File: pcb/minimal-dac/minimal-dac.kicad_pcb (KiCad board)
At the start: 6 parts, among them J1 PinHeader_2x06_P2.54mm, U1 AD5754

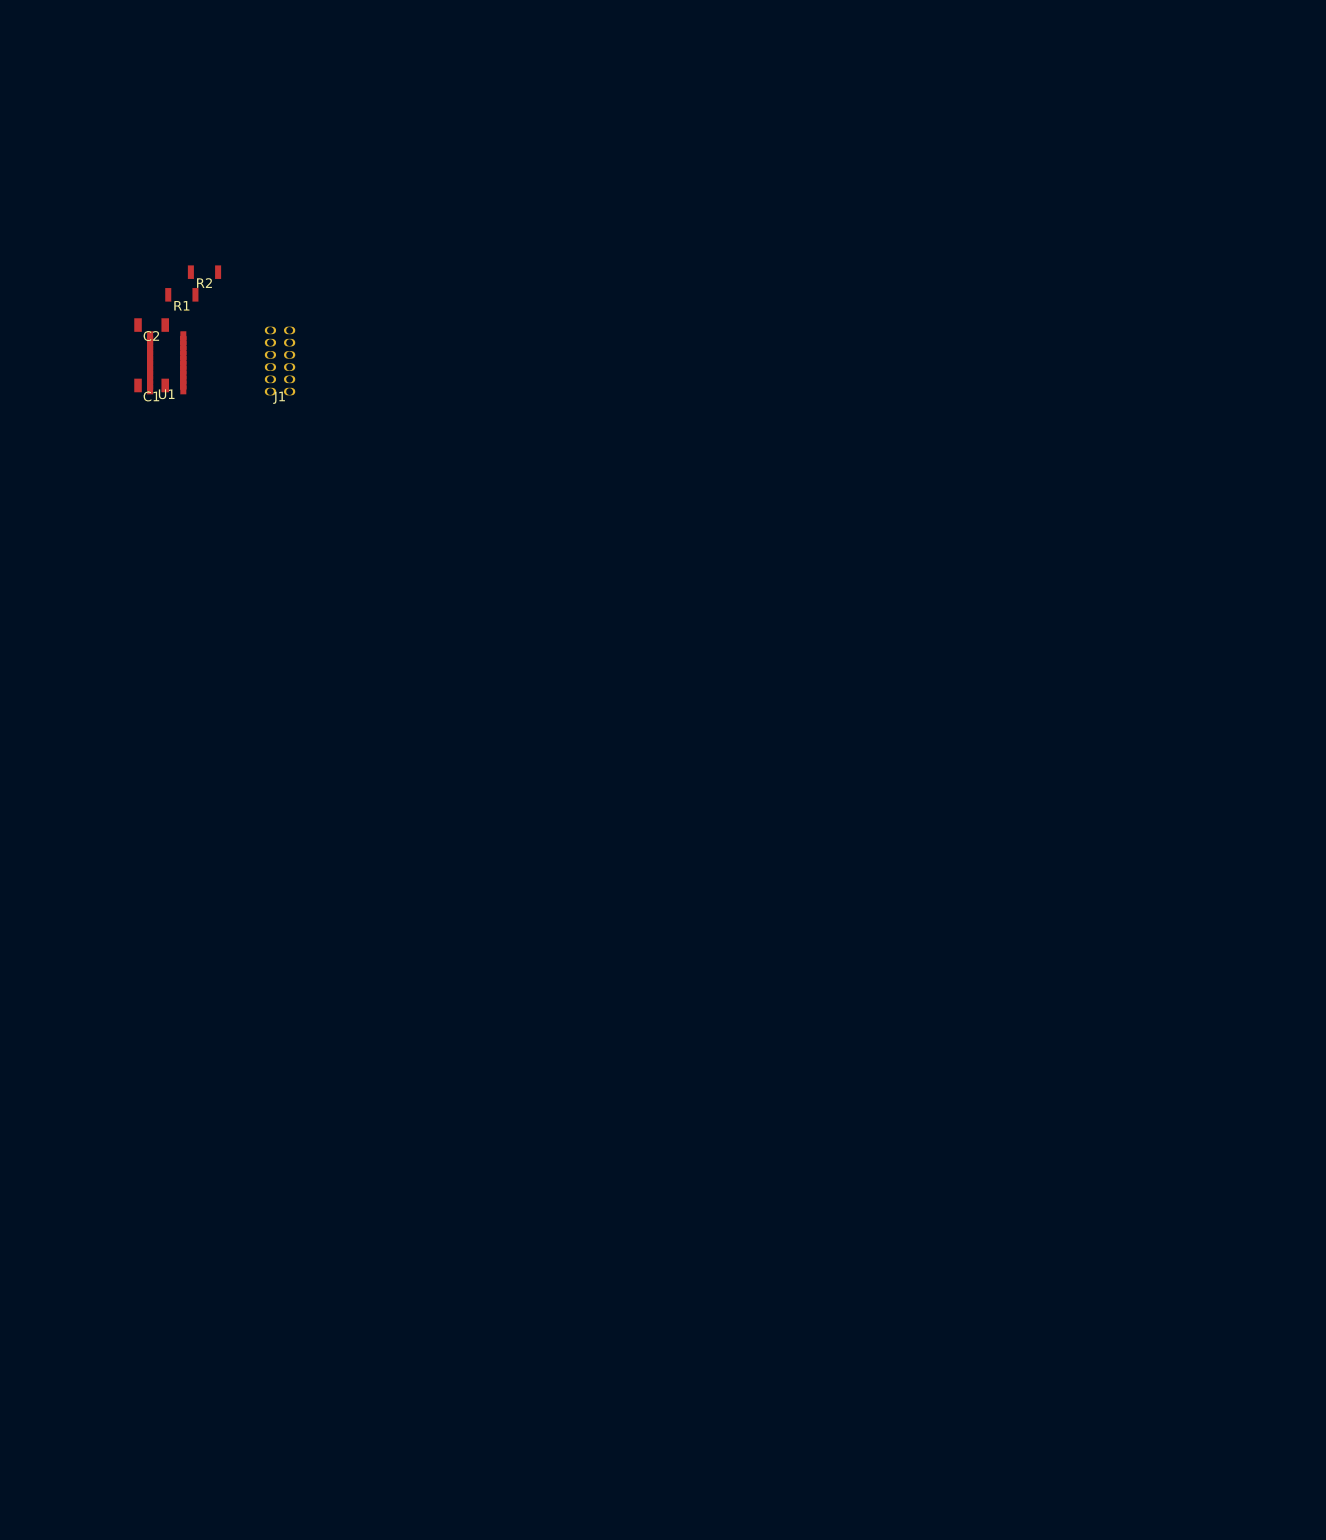
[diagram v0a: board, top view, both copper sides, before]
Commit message: AD5754 pcb en elements gedachten
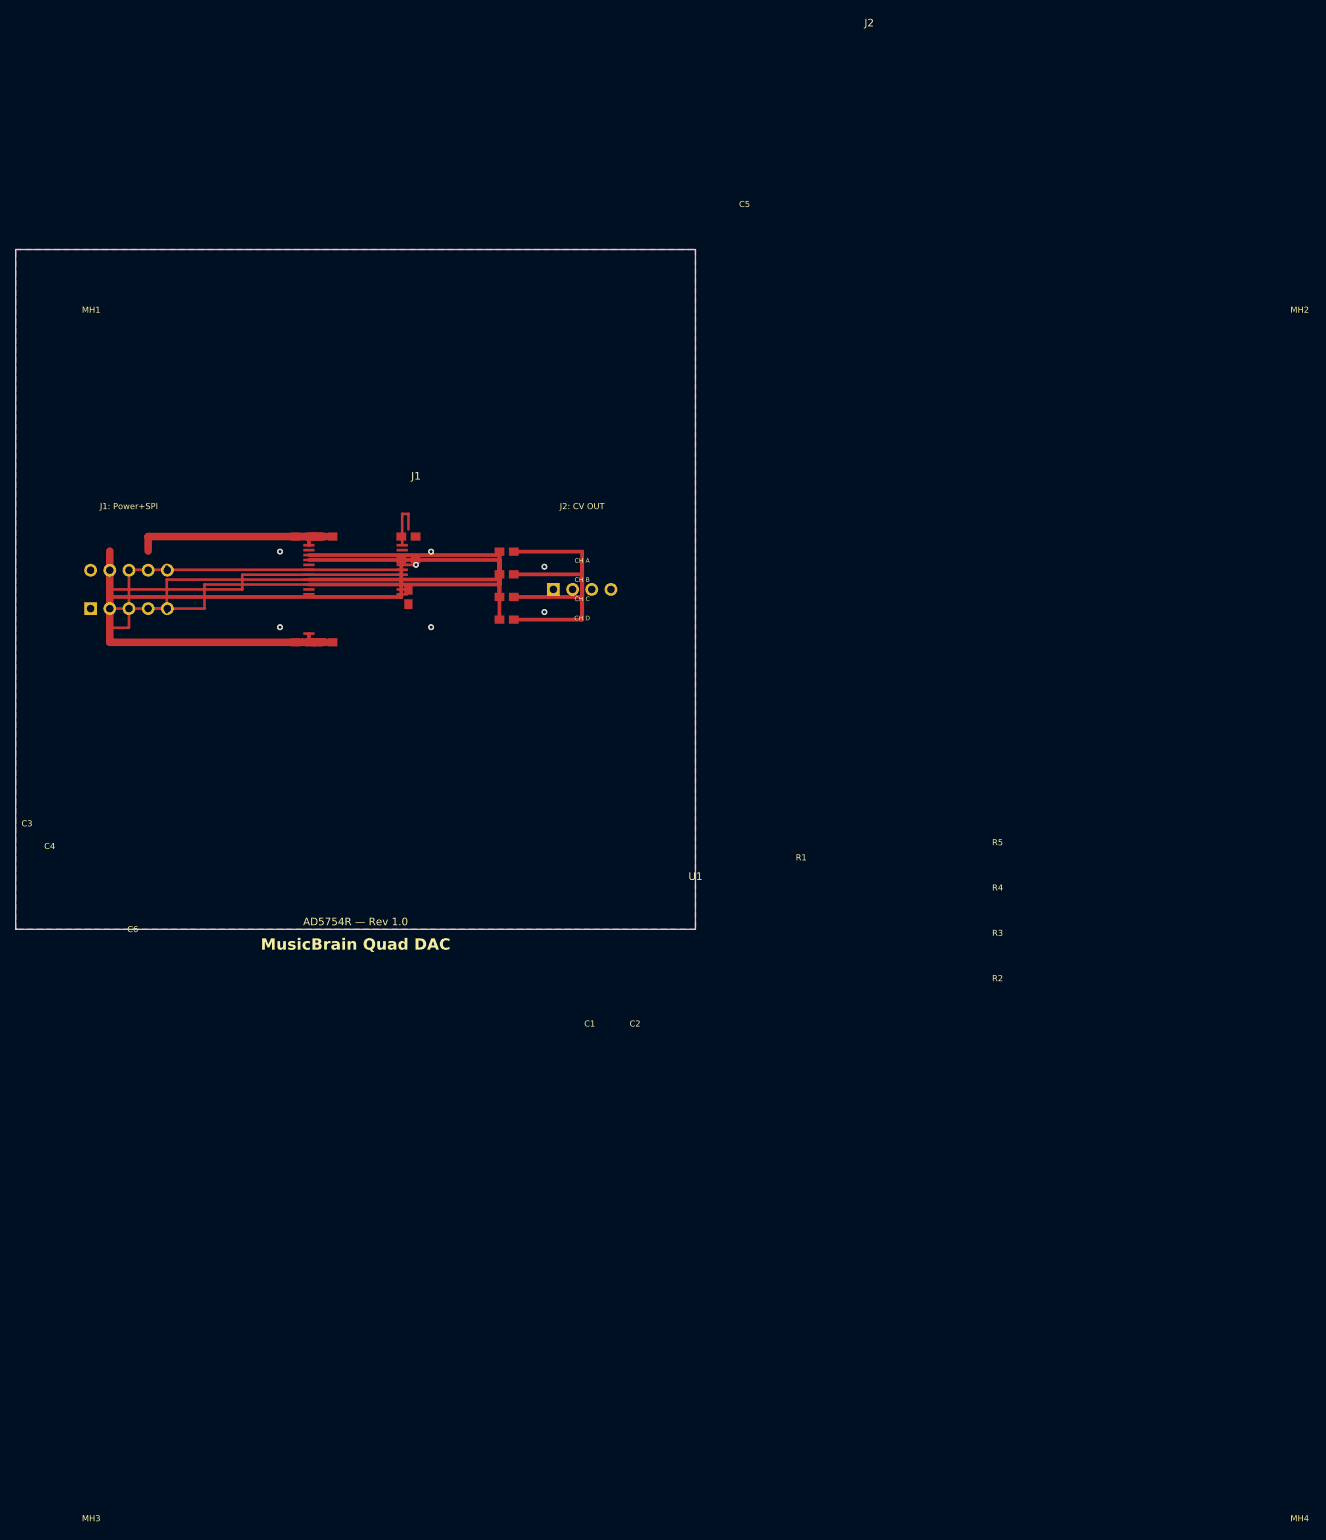
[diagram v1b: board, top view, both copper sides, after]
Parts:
- added C3: 10µF, Capacitor_SMD:C_0805_2012Metric, F.Cu at (38.0, 38.0)
- added C4: 0.1µF, Capacitor_SMD:C_0805_2012Metric, F.Cu at (41.0, 38.0)
- added C5: 0.1µF, Capacitor_SMD:C_0805_2012Metric, F.Cu at (52.0, 46.0)
- added C6: 0.1µF, Capacitor_SMD:C_0805_2012Metric, F.Cu at (52.0, 38.0)
- added J2: CV_OUT, Connector_PinHeader_2.54mm:PinHeader_1x04_P2.54mm_Vertical, F.Cu at (75.0, 45.0)
- added MH1: , MountingHole:MountingHole_3.2mm_M3, F.Cu at (5.00, 5.00)
- added MH2: , MountingHole:MountingHole_3.2mm_M3, F.Cu at (85.0, 5.00)
- added MH3: , MountingHole:MountingHole_3.2mm_M3, F.Cu at (5.00, 85.0)
- added MH4: , MountingHole:MountingHole_3.2mm_M3, F.Cu at (85.0, 85.0)
- added R3: 47Ω, Resistor_SMD:R_0805_2012Metric, F.Cu at (65.0, 46.0)
- added R4: 47Ω, Resistor_SMD:R_0805_2012Metric, F.Cu at (65.0, 43.0)
- added R5: 47Ω, Resistor_SMD:R_0805_2012Metric, F.Cu at (65.0, 40.0)
- C1: value 0.1uF -> 10µF
- C2: value 10uF -> 0.1µF
- J1: value PinHeader_2x06_P2.54mm -> Power+SPI; footprint Connector_PinHeader_2.54mm:PinHeader_2x06_P2.54mm_Vertical -> Connector_PinHeader_2.54mm:PinHeader_2x05_P2.54mm_Vertical
- R1: value 10k -> 10kΩ
- R2: value 47R -> 47Ω
- U1: value AD5754 -> AD5754R
- moved R2 61.0 mm to (65.0, 49.0)
- moved C2 47.9 mm to (41.0, 52.0)
- moved R1 46.1 mm to (52.0, 41.0)
- moved C1 39.4 mm to (38.0, 52.0)
- moved U1 39.1 mm to (45.0, 45.0)
- moved J1 36.1 mm to (15.0, 45.0), turned to 90 degrees
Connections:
- C1 pad 1: +3V3 -> +12V
- J1 pad 10: VOUT_B -> GND
- J1 pad 3: GND -> +3V3
- J1 pad 4: +3V3 -> GND
- J1 pad 5: SCK -> MOSI
- J1 pad 6: MOSI -> GND
- J1 pad 7: MISO -> SCK
- J1 pad 8: CS -> MISO
- J1 pad 9: VOUT_A -> CS
- R1 pad 1: CLR -> +3V3
- R1 pad 2: +3V3 -> CLR
- R2 pad 2: GND -> VOUT_A
- U1 pad 14: GND -> SCK
- U1 pad 15: REFIN -> MISO
- U1 pad 16: GND -> MOSI
- U1 pad 20: GND -> (no net)
- U1 pad 22: SCK -> REFIN
- U1 pad 23: MISO -> GND
- U1 pad 24: MOSI -> +12V
- U1 pad 7: VOUT_C -> (no net)
- U1 pad 8: VOUT_D -> VOUT_C
- U1 pad 9: (no net) -> VOUT_D
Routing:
- net VOUT_A: track 0.00 -> 50.6 mm
- net +3V3: track 0.00 -> 47.6 mm
- net VOUT_D: track 0.00 -> 47.4 mm
- net CS: track 0.00 -> 46.4 mm
- net +12V: track 0.00 -> 43.9 mm
- net SCK: track 0.00 -> 41.9 mm
- net VOUT_B: track 0.00 -> 41.4 mm
- net MOSI: track 0.00 -> 40.7 mm
- net VOUT_C: track 0.00 -> 38.2 mm
- net MISO: track 0.00 -> 37.5 mm
- net -12V: track 0.00 -> 28.7 mm
- net REFIN: track 0.00 -> 7.02 mm
- net CLR: track 0.00 -> 1.88 mm
- net GND: track 0.00 -> 1.83 mm, vias 0 -> 9
- added copper zone on B.Cu, net GND
- added copper zone on F.Cu, net GND
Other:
- board outline added: 90 x 90 mm
- copper layers 0 -> 2
- rule pad_to_mask_clearance: 0.04 -> 0.05
- board text added: "AD5754R — Rev 1.0"
- board text added: "CH A"
- board text added: "CH B"
- board text added: "CH C"
- board text added: "CH D"
- board text added: "J1: Power+SPI"
- board text added: "J2: CV OUT"
- board text added: "JLCPCB 2-layer 1.6mm FR4"
- board text added: "MusicBrain Quad DAC"

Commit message: pcbs
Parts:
- U1: value AD5754R -> AD5754BREZ
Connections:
- U1 pad 11: GND -> CLR
- U1 pad 12: +3V3 -> (no net)
- U1 pad 13: GND -> (no net)
- U1 pad 14: SCK -> +3V3
- U1 pad 15: MISO -> GND
- U1 pad 16: MOSI -> MISO
- U1 pad 17: CS -> REFIN
- U1 pad 19: CLR -> GND
- U1 pad 2: GND -> (no net)
- U1 pad 20: (no net) -> GND
- U1 pad 22: REFIN -> VOUT_D
- U1 pad 23: GND -> VOUT_C
- U1 pad 7: (no net) -> CS
- U1 pad 8: VOUT_C -> SCK
- U1 pad 9: VOUT_D -> MOSI
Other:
- board text added: "AD5754BREZ — Rev 1.0"
- board text removed: "AD5754R — Rev 1.0"
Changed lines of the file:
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@@
   (layers
     (0 "F.Cu" signal)
-    (1 "In1.Cu" dielectric 1)
-    (2 "In2.Cu" dielectric 2)
+    (1 "In1.Cu" dielectric)
+    (2 "In2.Cu" dielectric)
     (3 "B.Cu" signal)
     (4 "F.Adhes" user "Adhesive on front")
@@
   ;; Footprints
   ;; =========================================================================
-  ;; ── U1: AD5754R — TSSOP-24 ────────────────────────────────────────────
+  ;; ── U1: AD5754BREZ — TSSOP-24 ────────────────────────────────────────────
   (footprint "Package_SO:TSSOP-24_4.4x7.8mm_P0.65mm"
     (layer "F.Cu")
@@
     (property "Reference" "U1" (at 45 38 0) (layer "F.SilkS")
       (effects (font (size 1.0 1.0) (thickness 0.15))))
-    (property "Value" "AD5754R" (at 45 52 0) (layer "F.Fab")
+    (property "Value" "AD5754BREZ" (at 45 52 0) (layer "F.Fab")
       (effects (font (size 1.0 1.0) (thickness 0.15))))
     (pad "1" smd rect (at -6.175 -5.85 0) (size 1.5 0.35) (layers "F.Cu" "F.Paste" "F.Mask") (net 2))
-    (pad "2" smd rect (at -6.175 -5.2 0) (size 1.5 0.35) (layers "F.Cu" "F.Paste" "F.Mask") (net 4))
+    (pad "2" smd rect (at -6.175 -5.2 0) (size 1.5 0.35) (layers "F.Cu" "F.Paste" "F.Mask") (net 0))
     (pad "3" smd rect (at -6.175 -4.55 0) (size 1.5 0.35) (layers "F.Cu" "F.Paste" "F.Mask") (net 9))
     (pad "4" smd rect (at -6.175 -3.9 0) (size 1.5 0.35) (layers "F.Cu" "F.Paste" "F.Mask") (net 10))
     (pad "5" smd rect (at -6.175 -3.25 0) (size 1.5 0.35) (layers "F.Cu" "F.Paste" "F.Mask") (net 0))
     (pad "6" smd rect (at -6.175 -2.6 0) (size 1.5 0.35) (layers "F.Cu" "F.Paste" "F.Mask") (net 0))
-    (pad "7" smd rect (at -6.175 -1.95 0) (size 1.5 0.35) (layers "F.Cu" "F.Paste" "F.Mask") (net 0))
-    (pad "8" smd rect (at -6.175 -1.3 0) (size 1.5 0.35) (layers "F.Cu" "F.Paste" "F.Mask") (net 11))
-    (pad "9" smd rect (at -6.175 -0.65 0) (size 1.5 0.35) (layers "F.Cu" "F.Paste" "F.Mask") (net 12))
+    (pad "7" smd rect (at -6.175 -1.95 0) (size 1.5 0.35) (layers "F.Cu" "F.Paste" "F.Mask") (net 8))
+    (pad "8" smd rect (at -6.175 -1.3 0) (size 1.5 0.35) (layers "F.Cu" "F.Paste" "F.Mask") (net 6))
+    (pad "9" smd rect (at -6.175 -0.65 0) (size 1.5 0.35) (layers "F.Cu" "F.Paste" "F.Mask") (net 5))
     (pad "10" smd rect (at -6.175 0.0 0) (size 1.5 0.35) (layers "F.Cu" "F.Paste" "F.Mask") (net 4))
-    (pad "11" smd rect (at -6.175 0.65 0) (size 1.5 0.35) (layers "F.Cu" "F.Paste" "F.Mask") (net 4))
-    (pad "12" smd rect (at 6.175 0.65 0) (size 1.5 0.35) (layers "F.Cu" "F.Paste" "F.Mask") (net 3))
-    (pad "13" smd rect (at 6.175 0.0 0) (size 1.5 0.35) (layers "F.Cu" "F.Paste" "F.Mask") (net 4))
-    (pad "14" smd rect (at 6.175 -0.65 0) (size 1.5 0.35) (layers "F.Cu" "F.Paste" "F.Mask") (net 6))
-    (pad "15" smd rect (at 6.175 -1.3 0) (size 1.5 0.35) (layers "F.Cu" "F.Paste" "F.Mask") (net 7))
-    (pad "16" smd rect (at 6.175 -1.95 0) (size 1.5 0.35) (layers "F.Cu" "F.Paste" "F.Mask") (net 5))
-    (pad "17" smd rect (at 6.175 -2.6 0) (size 1.5 0.35) (layers "F.Cu" "F.Paste" "F.Mask") (net 8))
+    (pad "11" smd rect (at -6.175 0.65 0) (size 1.5 0.35) (layers "F.Cu" "F.Paste" "F.Mask") (net 14))
+    (pad "12" smd rect (at 6.175 0.65 0) (size 1.5 0.35) (layers "F.Cu" "F.Paste" "F.Mask") (net 0))
+    (pad "13" smd rect (at 6.175 0.0 0) (size 1.5 0.35) (layers "F.Cu" "F.Paste" "F.Mask") (net 0))
+    (pad "14" smd rect (at 6.175 -0.65 0) (size 1.5 0.35) (layers "F.Cu" "F.Paste" "F.Mask") (net 3))
+    (pad "15" smd rect (at 6.175 -1.3 0) (size 1.5 0.35) (layers "F.Cu" "F.Paste" "F.Mask") (net 4))
+    (pad "16" smd rect (at 6.175 -1.95 0) (size 1.5 0.35) (layers "F.Cu" "F.Paste" "F.Mask") (net 7))
+    (pad "17" smd rect (at 6.175 -2.6 0) (size 1.5 0.35) (layers "F.Cu" "F.Paste" "F.Mask") (net 13))
     (pad "18" smd rect (at 6.175 -3.25 0) (size 1.5 0.35) (layers "F.Cu" "F.Paste" "F.Mask") (net 4))
-    (pad "19" smd rect (at 6.175 -3.9 0) (size 1.5 0.35) (layers "F.Cu" "F.Paste" "F.Mask") (net 14))
-    (pad "20" smd rect (at 6.175 -4.55 0) (size 1.5 0.35) (layers "F.Cu" "F.Paste" "F.Mask") (net 0))
+    (pad "19" smd rect (at 6.175 -3.9 0) (size 1.5 0.35) (layers "F.Cu" "F.Paste" "F.Mask") (net 4))
+    (pad "20" smd rect (at 6.175 -4.55 0) (size 1.5 0.35) (layers "F.Cu" "F.Paste" "F.Mask") (net 4))
     (pad "21" smd rect (at 6.175 -5.2 0) (size 1.5 0.35) (layers "F.Cu" "F.Paste" "F.Mask") (net 4))
-    (pad "22" smd rect (at 6.175 -5.85 0) (size 1.5 0.35) (layers "F.Cu" "F.Paste" "F.Mask") (net 13))
-    (pad "23" smd rect (at -6.175 0.65 0) (size 1.5 0.35) (layers "F.Cu" "F.Paste" "F.Mask") (net 4))
+    (pad "22" smd rect (at 6.175 -5.85 0) (size 1.5 0.35) (layers "F.Cu" "F.Paste" "F.Mask") (net 12))
+    (pad "23" smd rect (at -6.175 0.65 0) (size 1.5 0.35) (layers "F.Cu" "F.Paste" "F.Mask") (net 11))
     (pad "24" smd rect (at -6.175 5.85 0) (size 1.5 0.35) (layers "F.Cu" "F.Paste" "F.Mask") (net 1))
   )
@@
   (segment (start 41 38) (end 38.825 38) (width 1.0) (layer "F.Cu") (net 2))
   (segment (start 38.825 38) (end 38.825 39.15) (width 0.5) (layer "F.Cu") (net 2))
-  ;; +3V3 — J1.3 → C5 → R1 → U1.12 (DVCC) (+ CLR pull-up)
+  ;; +3V3 — J1.3 → C5 → R1 → U1.14 (DVCC) (+ CLR pull-up)
   (segment (start 12.46 42.46) (end 12.46 46) (width 0.5) (layer "F.Cu") (net 3))
   (segment (start 12.46 46) (end 51.05 46) (width 0.5) (layer "F.Cu") (net 3))
@@
   (segment (start 51.05 41) (end 51.05 41) (width 0.5) (layer "F.Cu") (net 3))
   (segment (start 51.05 45.65) (end 51.175 45.65) (width 0.35) (layer "F.Cu") (net 3))
-  ;; CLR pull-up — R1.2 → U1.19 (CLR)
+  ;; CLR pull-up — R1.2 → U1.11 (CLR)
   (segment (start 52.95 41) (end 52.95 41.1) (width 0.35) (layer "F.Cu") (net 14))
   (segment (start 52.95 41.1) (end 51.175 41.1) (width 0.35) (layer "F.Cu") (net 14))
@@
     )
   )
-  ;; MOSI — J1.5 → U1.16 (SDIN)
+  ;; MOSI — J1.5 → U1.9 (SDIN)
   (segment (start 12.46 45) (end 30 45) (width 0.35) (layer "F.Cu") (net 5))
   (segment (start 30 45) (end 30 43.05) (width 0.35) (layer "F.Cu") (net 5))
   (segment (start 30 43.05) (end 51.175 43.05) (width 0.35) (layer "F.Cu") (net 5))
-  ;; SCK — J1.7 → U1.14 (SCLK)
+  ;; SCK — J1.7 → U1.8 (SCLK)
   (segment (start 12.46 47.54) (end 25 47.54) (width 0.35) (layer "F.Cu") (net 6))
   (segment (start 25 47.54) (end 25 44.35) (width 0.35) (layer "F.Cu") (net 6))
   (segment (start 25 44.35) (end 51.175 44.35) (width 0.35) (layer "F.Cu") (net 6))
-  ;; MISO — J1.8 → U1.15 (SDO)
+  ;; MISO — J1.8 → U1.16 (SDO)
   (segment (start 17.54 47.54) (end 20 47.54) (width 0.35) (layer "F.Cu") (net 7))
   (segment (start 20 47.54) (end 20 43.7) (width 0.35) (layer "F.Cu") (net 7))
   (segment (start 20 43.7) (end 51.175 43.7) (width 0.35) (layer "F.Cu") (net 7))
-  ;; CS — J1.9 → U1.17 (SYNC)
+  ;; CS — J1.9 → U1.7 (SYNC)
   (segment (start 12.46 50.08) (end 15 50.08) (width 0.35) (layer "F.Cu") (net 8))
   (segment (start 15 50.08) (end 15 42.4) (width 0.35) (layer "F.Cu") (net 8))
   (segment (start 15 42.4) (end 51.175 42.4) (width 0.35) (layer "F.Cu") (net 8))
-  ;; REFIN — C6.2 → U1.22 (REFIN/REFOUT)
+  ;; REFIN — C6.2 → U1.17 (REFIN)
   (segment (start 52 37.05) (end 52 35) (width 0.35) (layer "F.Cu") (net 13))
   (segment (start 52 35) (end 51.175 35) (width 0.35) (layer "F.Cu") (net 13))
@@
   (segment (start 65.95 46) (end 75 46) (width 0.5) (layer "F.Cu") (net 10))
   (segment (start 75 46) (end 75 43.73) (width 0.5) (layer "F.Cu") (net 10))
-  ;; VOUT_C — U1.8 → R4 → J2.3
+  ;; VOUT_C — U1.23 → R4 → J2.3
   (segment (start 38.825 43.7) (end 64.05 43.7) (width 0.5) (layer "F.Cu") (net 11))
   (segment (start 64.05 43.7) (end 64.05 43) (width 0.5) (layer "F.Cu") (net 11))
   (segment (start 65.95 43) (end 75 43) (width 0.5) (layer "F.Cu") (net 11))
   (segment (start 75 43) (end 75 46.27) (width 0.5) (layer "F.Cu") (net 11))
-  ;; VOUT_D — U1.9 → R5 → J2.4
+  ;; VOUT_D — U1.22 → R5 → J2.4
   (segment (start 38.825 44.35) (end 64.05 44.35) (width 0.5) (layer "F.Cu") (net 12))
   (segment (start 64.05 44.35) (end 64.05 40) (width 0.5) (layer "F.Cu") (net 12))
   (segment (start 65.95 40) (end 75 40) (width 0.5) (layer "F.Cu") (net 12))
   (segment (start 75 40) (end 75 48.81) (width 0.5) (layer "F.Cu") (net 12))
-  ;; LDAC — U1.18 → GND
+  ;; LDAC — U1.10 → GND
   (segment (start 51.175 41.75) (end 53 41.75) (width 0.35) (layer "F.Cu") (net 4))
   ;; Via to GND pour
@@
   (gr_text "MusicBrain Quad DAC" (at 45 92 0) (layer "F.SilkS")
     (effects (font (size 1.5 1.5) (thickness 0.2) (bold yes))))
-  (gr_text "AD5754R — Rev 1.0" (at 45 89 0) (layer "F.SilkS")
+  (gr_text "AD5754BREZ — Rev 1.0" (at 45 89 0) (layer "F.SilkS")
     (effects (font (size 1.0 1.0) (thickness 0.15))))
   (gr_text "J1: Power+SPI" (at 15 34 0) (layer "F.SilkS")
